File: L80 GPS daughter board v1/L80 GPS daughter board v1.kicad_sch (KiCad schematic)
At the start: 12 parts, among them J1 Conn_01x06_Socket, U1 AP2112K-3.3, U2 L80-R, U3 MCP73831-2-OT

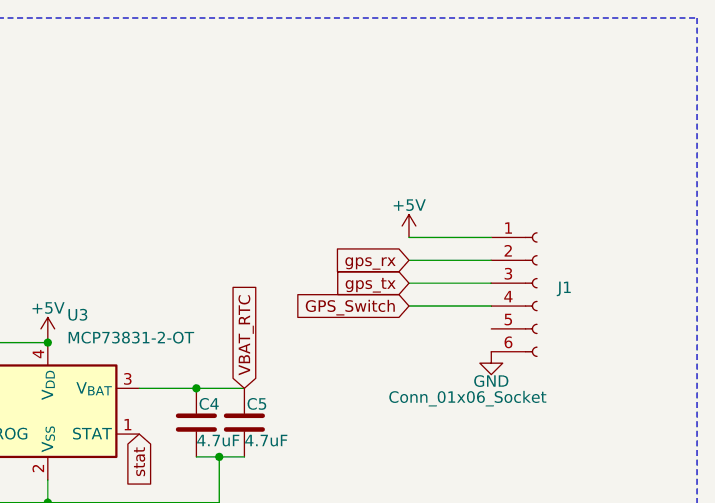
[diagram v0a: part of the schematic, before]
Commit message: routed the l80 gps daughter board and a few more modifications
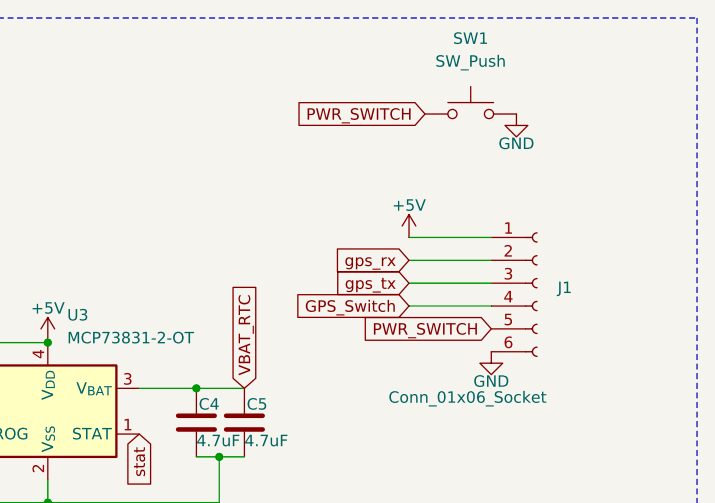
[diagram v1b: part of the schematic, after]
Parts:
- added SW1: SW_Push, Button_Switch_THT:SW_Tactile_SPST_Angled_PTS645Vx39-2LFS, symbol Switch:SW_Push
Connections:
- net GND: now also SW1.2
- net PWR_SWITCH: now reaches J1.5 (Pin_5)
- net PWR_SWITCH: now also SW1.1
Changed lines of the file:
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@@
+		)
+	)
+	(global_label "PWR_SWITCH"
+		(shape input)
+		(at 236.474 98.298 180)
+		(fields_autoplaced yes)
+		(effects
+			(font
+				(size 1.27 1.27)
+			)
+			(justify right)
+		)
+		(property "Intersheetrefs" "${INTERSHEET_REFS}"
+			(at 221.696 98.298 0)
+			(effects
+				(font
+					(size 1.27 1.27)
+				)
+				(justify right)
+				(hide yes)
+			)
 		)
 	)
@@
 		)
 	)
+	(global_label "PWR_SWITCH"
+		(shape input)
+		(at 229.108 74.422 180)
+		(fields_autoplaced yes)
+		(effects
+			(font
+				(size 1.27 1.27)
+			)
+			(justify right)
+		)
+		(property "Intersheetrefs" "${INTERSHEET_REFS}"
+			(at 214.33 74.422 0)
+			(effects
+				(font
+					(size 1.27 1.27)
+				)
+				(justify right)
+				(hide yes)
+			)
+		)
+	)
 	(symbol
 		(lib_id "Battery_Management:MCP73831-2-OT")
@@
 	)
 	(symbol
+		(lib_id "power:GND")
+		(at 239.268 74.422 0)
+		(unit 1)
+		(exclude_from_sim no)
+		(in_bom yes)
+		(on_board yes)
+		(dnp no)
+		(property "Reference" "#PWR012"
+			(at 239.268 80.772 0)
+			(effects
+				(font
+					(size 1.27 1.27)
+				)
+				(hide yes)
+			)
+		)
+		(property "Value" "GND"
+			(at 239.268 77.724 0)
+			(effects
+				(font
+					(size 1.27 1.27)
+				)
+			)
+		)
+		(property "Footprint" ""
+			(at 239.268 74.422 0)
+			(effects
+				(font
+					(size 1.27 1.27)
+				)
+				(hide yes)
+			)
+		)
+		(property "Datasheet" ""
+			(at 239.268 74.422 0)
+			(effects
+				(font
+					(size 1.27 1.27)
+				)
+				(hide yes)
+			)
+		)
+		(property "Description" ""
+			(at 239.268 74.422 0)
+			(effects
+				(font
+					(size 1.27 1.27)
+				)
+				(hide yes)
+			)
+		)
+		(pin "1"
+		)
+		(instances
+			(project "L80 GPS daughter board v1"
+				(path "/d19b7dbb-d08f-4a81-9071-b9150d5b9101"
+					(reference "#PWR012")
+					(unit 1)
+				)
+			)
+		)
+	)
+	(symbol
 		(lib_id "power:+5V")
 		(at 152.908 111.76 0)
@@
 					(unit 1)
 				)
+			)
+		)
+	)
+	(symbol
+		(lib_id "Switch:SW_Push")
+		(at 234.188 74.422 0)
+		(unit 1)
+		(exclude_from_sim no)
+		(in_bom yes)
+		(on_board yes)
+		(dnp no)
+		(fields_autoplaced yes)
+		(property "Reference" "SW1"
+			(at 234.188 66.04 0)
+			(effects
+				(font
+					(size 1.27 1.27)
+				)
+			)
+		)
+		(property "Value" "SW_Push"
+			(at 234.188 68.58 0)
+			(effects
+				(font
+					(size 1.27 1.27)
+				)
+			)
+		)
+		(property "Footprint" "Button_Switch_THT:SW_Tactile_SPST_Angled_PTS645Vx39-2LFS"
+			(at 234.188 69.342 0)
+			(effects
+				(font
+					(size 1.27 1.27)
+				)
+				(hide yes)
+			)
+		)
+		(property "Datasheet" "~"
+			(at 234.188 69.342 0)
+			(effects
+				(font
+					(size 1.27 1.27)
+				)
+				(hide yes)
+			)
+		)
+		(property "Description" "Push button switch, generic, two pins"
+			(at 234.188 74.422 0)
+			(effects
+				(font
+					(size 1.27 1.27)
+				)
+				(hide yes)
+			)
+		)
+		(pin "2"
+		)
+		(pin "1"
+		)
+		(instances
+			(project ""
+				(path "/d19b7dbb-d08f-4a81-9071-b9150d5b9101"
+					(reference "SW1")
+					(unit 1)
+				)

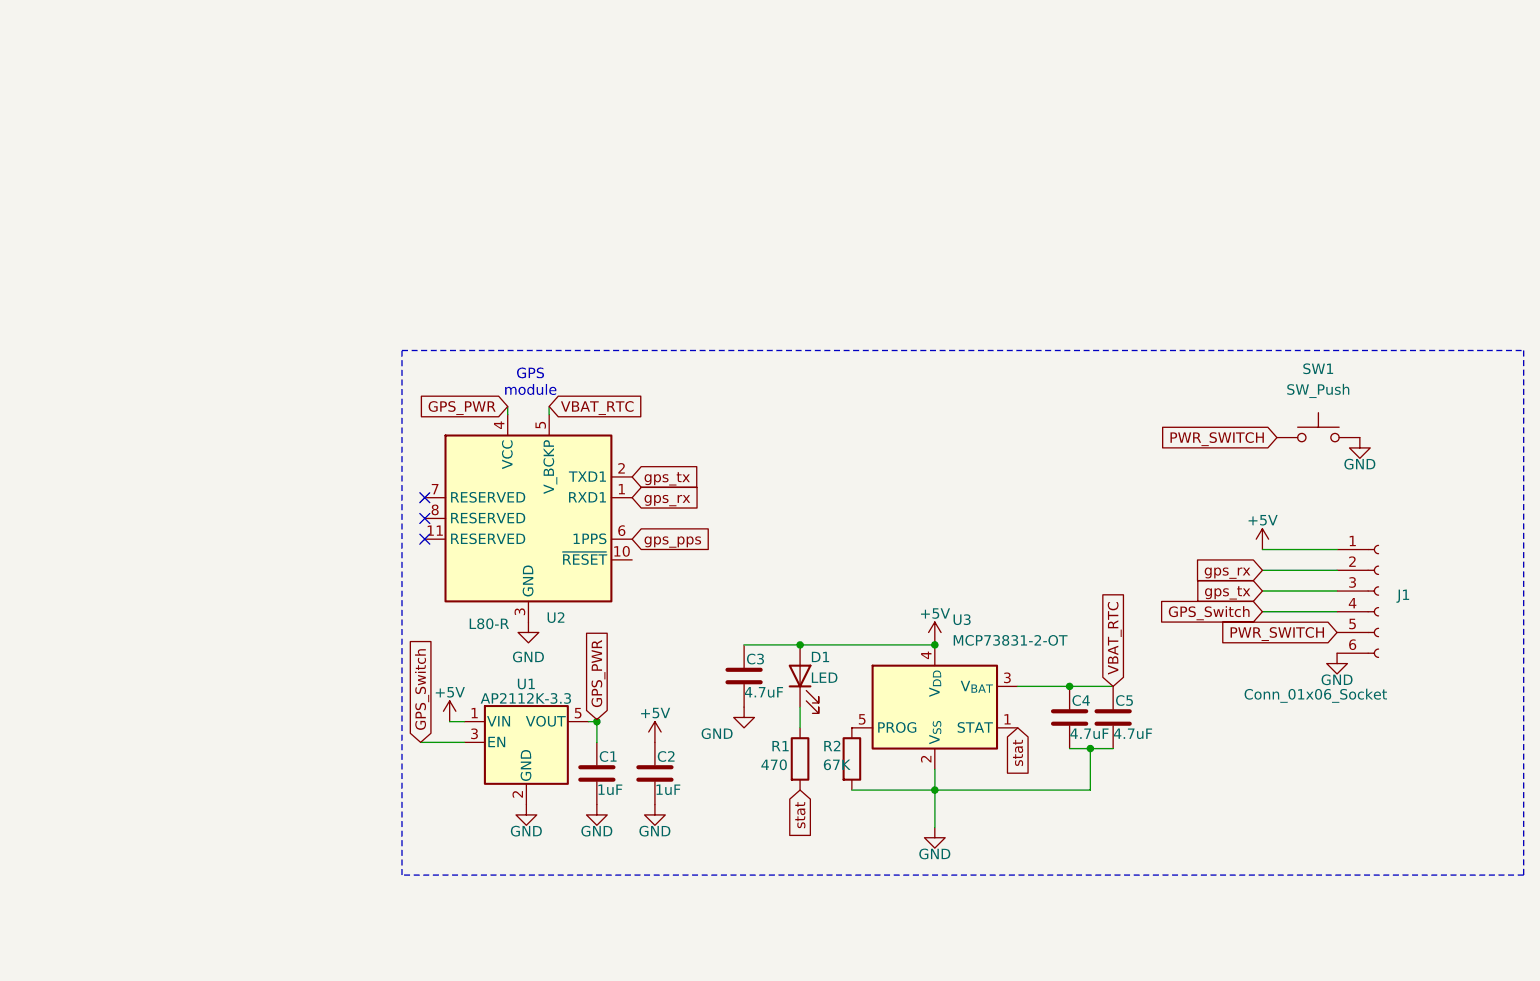
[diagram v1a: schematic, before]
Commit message: started on the enclosure designs
started on the enclosure designs
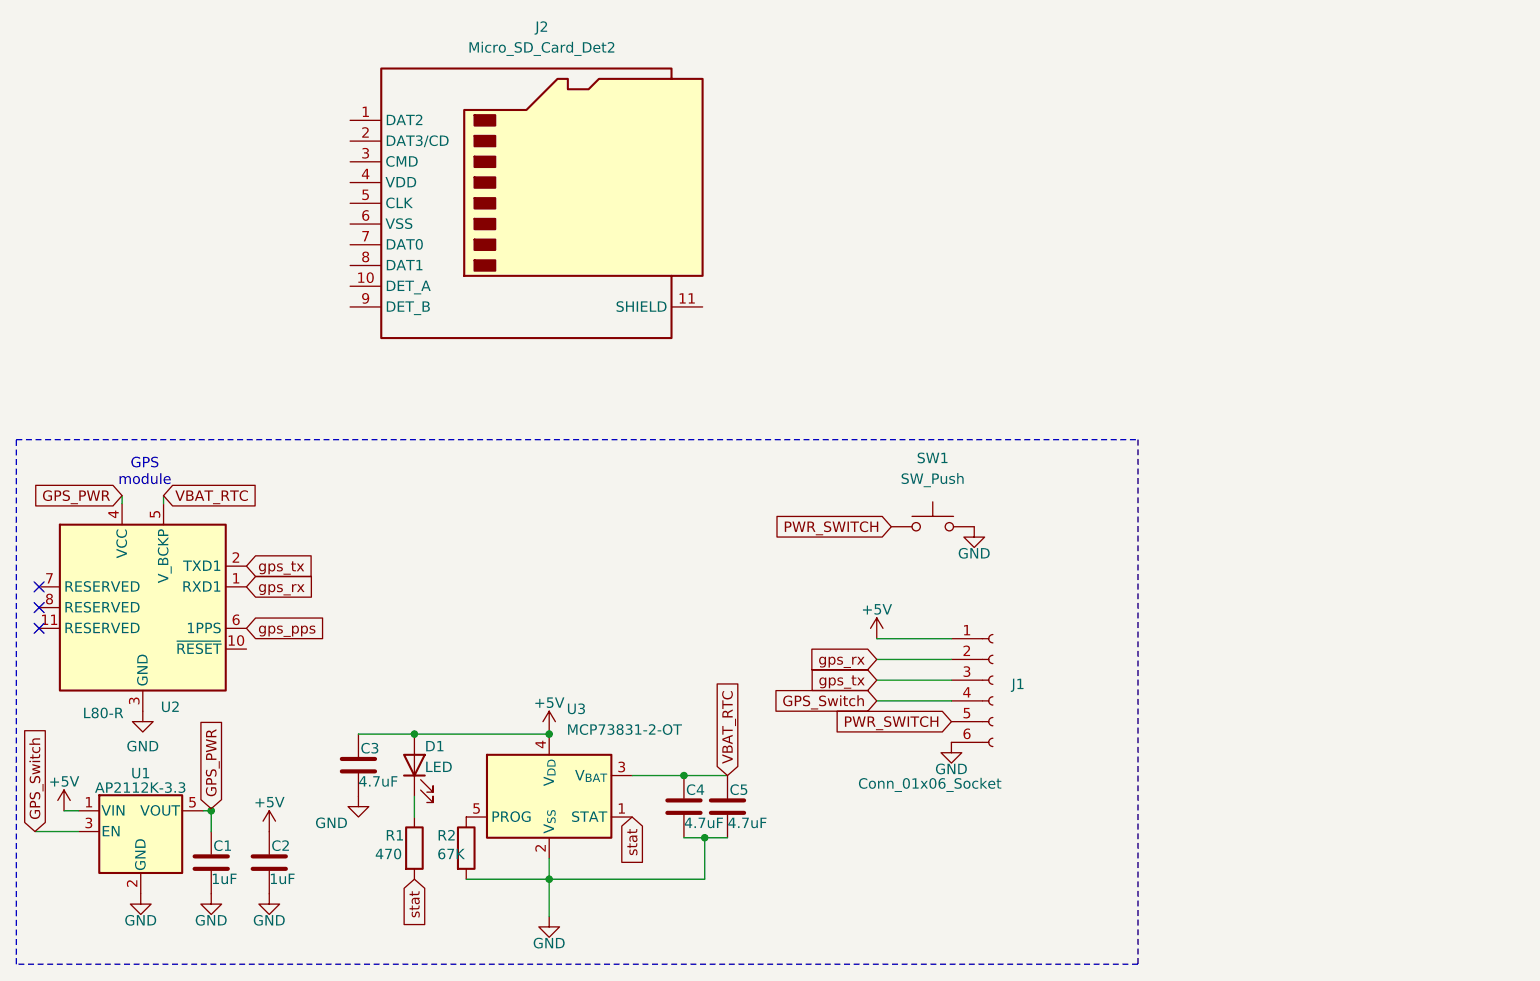
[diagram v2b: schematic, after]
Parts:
- added J2: Micro_SD_Card_Det2, Connector_Card:microSD_HC_Hirose_DM3BT-DSF-PEJS, symbol Connector:Micro_SD_Card_Det2
- J1: footprint Connector_PinHeader_2.54mm:PinHeader_1x06_P2.54mm_Horizontal -> Connector_PinHeader_2.54mm:PinHeader_1x06_P2.54mm_Vertical
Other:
- moved on the sheet: C1, C2, C3, C4, C5, D1, J1, R1, R2, SW1, U1, U2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
